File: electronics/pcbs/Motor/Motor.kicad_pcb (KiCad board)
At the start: 2 copper layers, 101.6 x 53.3 mm, 13 parts, among them P1 Digital, P10 CONN_01X01, P11 CONN_01X01, P12 CONN_01X01, P13 CONN_01X01, P2 Power, P3 Analog, P4 Analog, P5 PWM, P6 PWM, P7 Communication, P8 CONN_01X01, P9 CONN_01X01

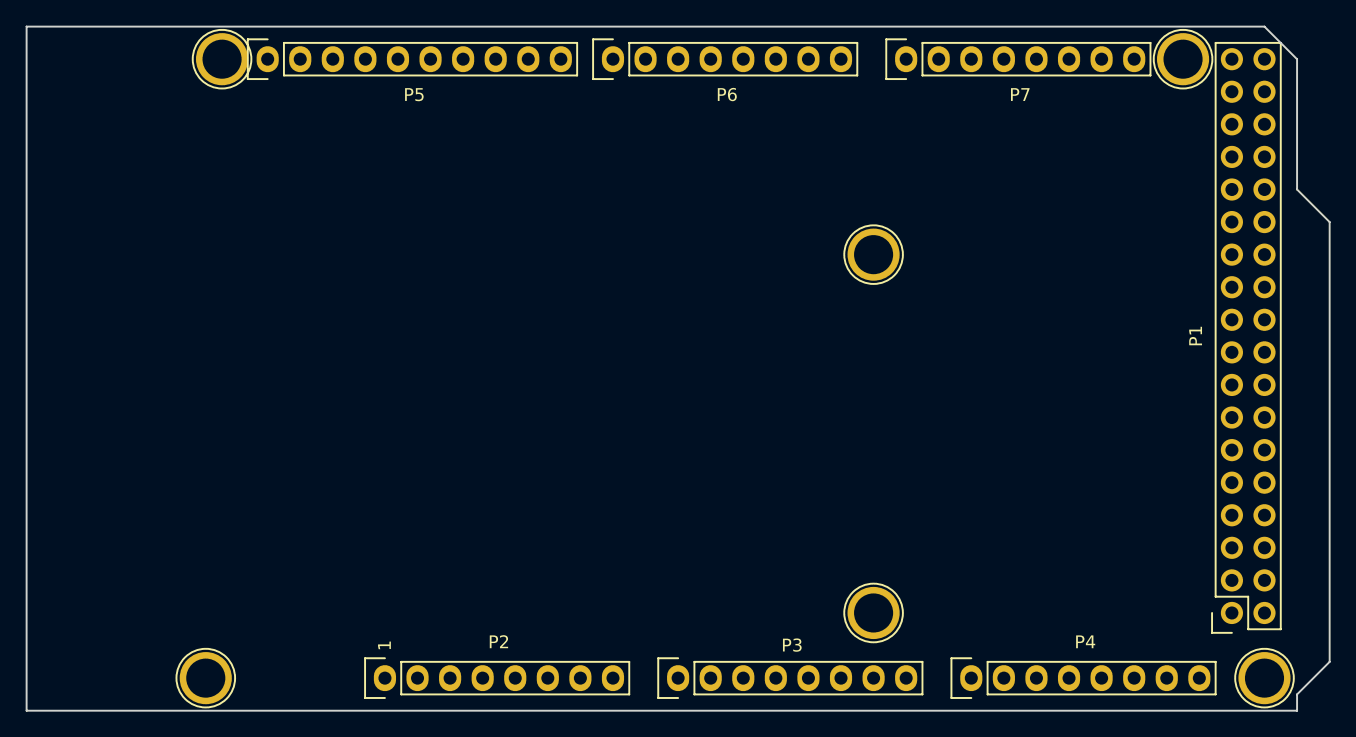
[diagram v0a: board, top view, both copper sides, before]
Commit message: Motor PCB: Redesigned PCB. Swapped pins for Encoder R's A and B so that layout was easier.
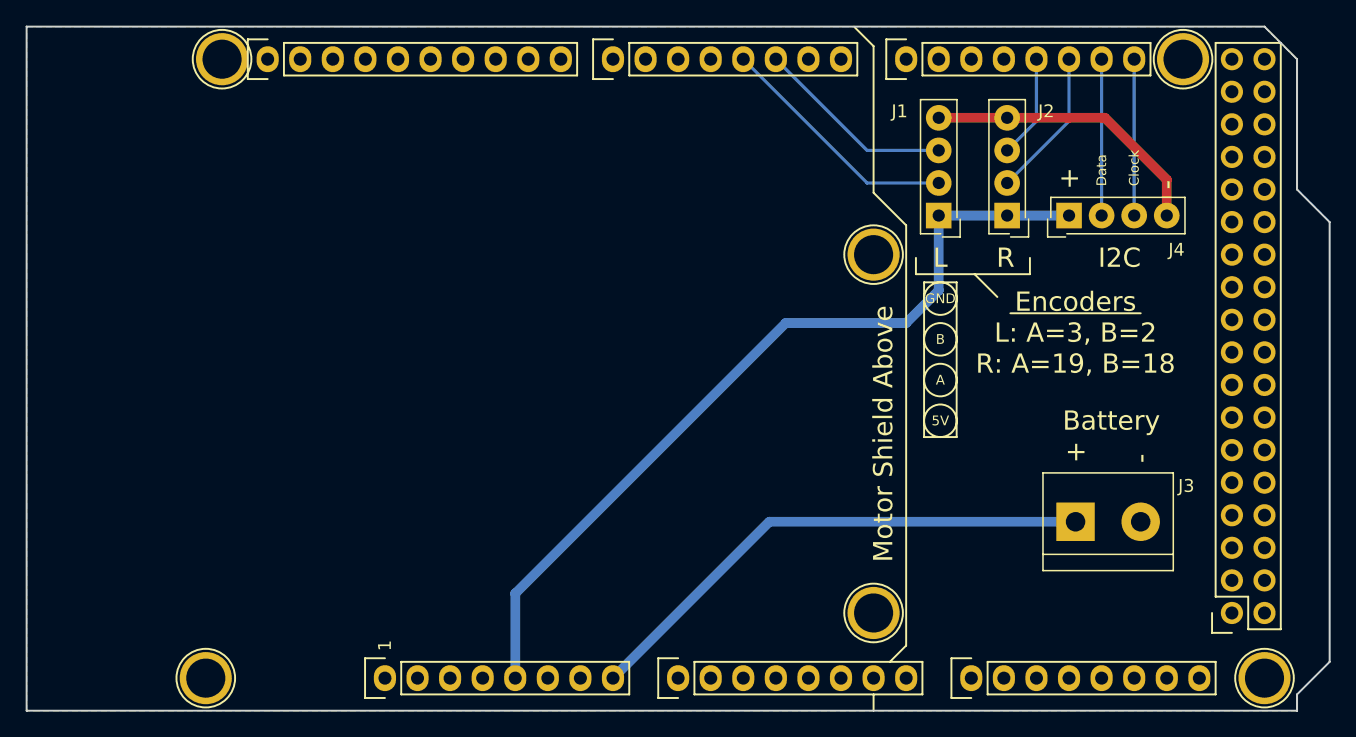
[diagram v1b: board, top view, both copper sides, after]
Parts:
- added J1: Left Encoder, Connectors_Samtec:SL-104-X-XX_1x04, F.Cu at (174.5, 83.1)
- added J2: Right Encoder, Connectors_Samtec:SL-104-X-XX_1x04, F.Cu at (179.8, 83.1)
- added J3: Battery, Connectors_Terminal_Blocks:TerminalBlock_bornier-2_P5.08mm, F.Cu at (185.2, 106.9)
- added J4: I2C, Connectors_Samtec:SL-104-X-XX_1x04, F.Cu at (184.7, 83.1)
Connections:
- net +3V3 renamed /+3.3V
- P10 pad 1: Net-(P10-Pad1) -> GND
- P11 pad 1: Net-(P11-Pad1) -> GND
- P12 pad 1: Net-(P12-Pad1) -> GND
- P13 pad 1: Net-(P13-Pad1) -> GND
- P2 pad 8: /Vin -> +BATT
- P8 pad 1: Net-(P8-Pad1) -> GND
- P9 pad 1: Net-(P9-Pad1) -> GND
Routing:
- net +5V: track 0.00 -> 65.4 mm
- net +BATT: track 0.00 -> 41.1 mm
- net GND: track 0.00 -> 22.6 mm
- net /3(**): track 0.00 -> 19.2 mm
- net /2(**): track 0.00 -> 15.6 mm
- net /21(SCL): track 0.00 -> 12.2 mm
- net /20(SDA): track 0.00 -> 12.2 mm
- net /19(Rx1): track 0.00 -> 11.7 mm
- net /18(Tx1): track 0.00 -> 8.06 mm
- added copper zone on B.Cu, net GND
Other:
- net class Ground added: clearance 0.2, trace_width 0.762, via_dia 1.8288, via_drill 1.2192
- net class Power added: clearance 0.2, trace_width 0.762, via_dia 1.8288, via_drill 1.2192
- board text added: "+"
- board text added: "-"
- board text added: "5V"
- board text added: "A"
- board text added: "B"
- board text added: "Battery"
- board text added: "Clock"
- board text added: "Data"
- board text added: "Encoders L: A=3, B=2 R: A=19, B=18"
- board text added: "GND"
- board text added: "I2C"
- board text added: "L"
- board text added: "Motor Shield Above"
- board text added: "R"
